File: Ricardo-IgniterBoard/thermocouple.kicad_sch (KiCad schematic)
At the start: 9 parts, among them U901 MAX31856

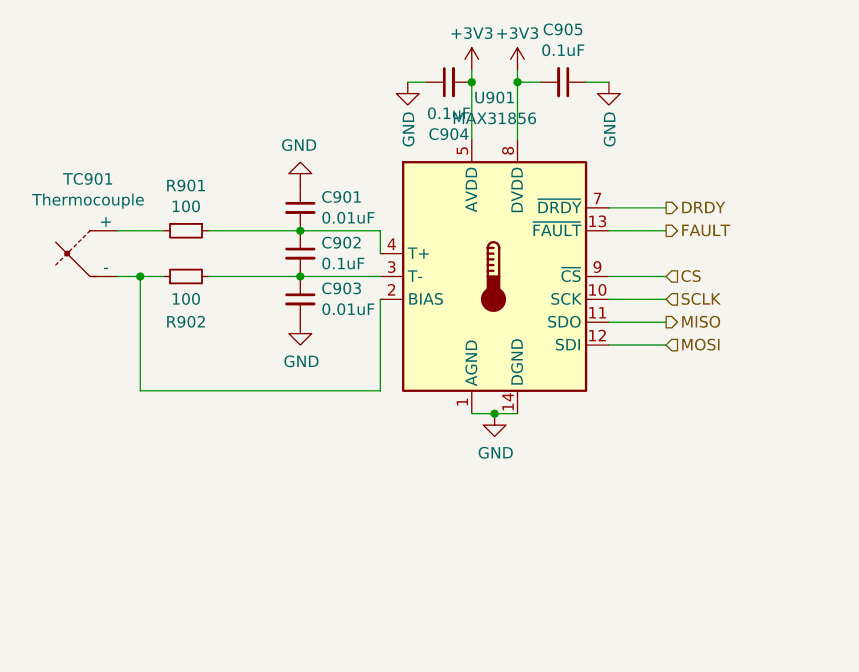
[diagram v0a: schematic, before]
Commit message: Fixed tc and igniter power
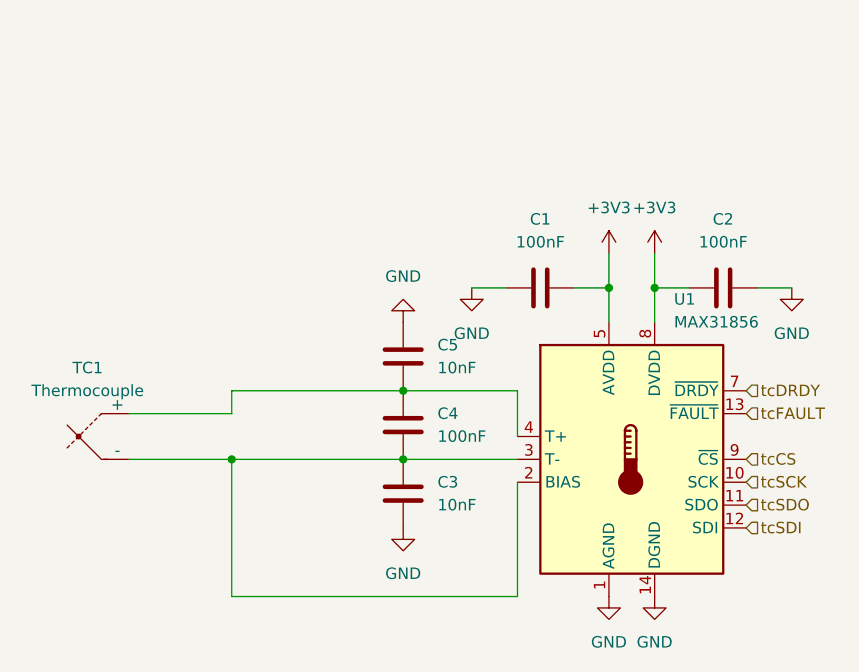
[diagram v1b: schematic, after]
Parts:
- removed C901, C903: 0.01uF, Capacitor_SMD:C_0402_1005Metric, symbol Device:C_Small
- removed C902, C904, C905: 0.1uF, Capacitor_SMD:C_0402_1005Metric, symbol Device:C_Small
- removed R901, R902: 100, Resistor_SMD:R_0402_1005Metric, symbol Device:R_Small
- removed TC901: Thermocouple, Connector_Molex:Molex_Nano-Fit_105313-xx02_1x02_P2.50mm_Horizontal, symbol Device:Thermocouple
- removed U901: MAX31856, Package_SO:TSSOP-14_4.4x5mm_P0.65mm, symbol Sensor_Temperature:MAX31856
- added C1, C2, C4: 100nF, symbol Device:C
- added C3, C5: 10nF, symbol Device:C
- added TC1: Thermocouple, symbol Device:Thermocouple
- added U1: MAX31856, Package_SO:TSSOP-14_4.4x5mm_P0.65mm, symbol Sensor_Temperature:MAX31856
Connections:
- net +3V3: now also C1.2, C2.2, U1.5 (AVDD), U1.8 (DVDD)
- net GND: now also C1.1, C2.1, C3.2, C5.1, U1.1 (AGND), U1.14 (DGND)
- new net: C4.1, C5.2, TC1.1 (+), U1.4 (T+)
- new net: C3.1, C4.2, TC1.2 (-), U1.2 (BIAS), U1.3 (T-)
- new net tcCS: U1.9 (~{CS})
- new net tcDRDY: U1.7 (~{DRDY})
- new net tcFAULT: U1.13 (~{FAULT})
- new net tcSCK: U1.10 (SCK)
- new net tcSDI: U1.12 (SDI)
- new net tcSDO: U1.11 (SDO)

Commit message: some more changes
added current sensor for solenoid, fixed optocouplers
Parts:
- C1, C2, C3, C4, C5: footprint (none) -> Capacitor_SMD:C_0402_1005Metric
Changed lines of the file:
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@@
 			)
 		)
-		(property "Footprint" ""
+		(property "Footprint" "Capacitor_SMD:C_0402_1005Metric"
 			(at 116.84 73.9648 0)
 			(effects
@@
 			)
 		)
-		(property "Footprint" ""
+		(property "Footprint" "Capacitor_SMD:C_0402_1005Metric"
 			(at 104.14 73.9648 0)
 			(effects
@@
 			)
 		)
-		(property "Footprint" ""
+		(property "Footprint" "Capacitor_SMD:C_0402_1005Metric"
 			(at 86.0552 86.36 0)
 			(effects
@@
 			)
 		)
-		(property "Footprint" ""
+		(property "Footprint" "Capacitor_SMD:C_0402_1005Metric"
 			(at 86.0552 93.98 0)
 			(effects
@@
 			)
 		)
-		(property "Footprint" ""
+		(property "Footprint" "Capacitor_SMD:C_0402_1005Metric"
 			(at 86.0552 101.6 0)
 			(effects

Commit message: Assigning footprints
and adding them to layout
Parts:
- TC1: footprint (none) -> Connector_Molex:Molex_Nano-Fit_105313-xx02_1x02_P2.50mm_Horizontal
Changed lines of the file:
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@@
 			)
 		)
-		(property "Footprint" ""
+		(property "Footprint" "Connector_Molex:Molex_Nano-Fit_105313-xx02_1x02_P2.50mm_Horizontal"
 			(at 37.465 90.17 0)
 			(effects
